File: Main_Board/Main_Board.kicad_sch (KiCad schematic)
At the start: 8 parts, among them U1 OKI-78SR-5_1.5-W36-C, U2 Teensy4.1_DEV-16771, U3 ATA6561

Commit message: **MAJOR CHANGES**
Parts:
- removed R1: 120ohm, symbol Device:R
- removed U3: ATA6561, Package_SO:SOIC-8_3.9x4.9mm_P1.27mm, symbol MRDT_Devices:ATA6561
- added 100nf: C, symbol Device:C
- added J1: RJ45_LED_Shielded, symbol Connector:RJ45_LED_Shielded
- added U3: AS5048A, Package_SO:TSSOP-14_4.4x5mm_P0.65mm, symbol Sensor_Magnetic:AS5048A
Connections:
- net +3.3V: no longer C2.1, C3.1, U1.3 (OUT)
- net GND: now also 100nf.2, J1.8, J1.9, J1.SH
- net LED: now reaches U2.LED
- net LED: now also J1.10
- net R+: now reaches U2.R+
- net R+: now also J1.4
- net R-: now reaches U2.R-
- net R-: now also J1.6
- net T+: now reaches U2.T+
- net T+: now also J1.1
- net T-: now reaches U2.T-
- net T-: now also J1.3
- net +12V renamed +36V
- net RXD1: no longer names the net of U2.0 (RX1)
- net RXD2: no longer names the net of U2.7 (RX2)
- net RXD3: no longer names the net of U2.28 (RX7)
- net STBY1: no longer names the net of U2.14 (A0)
- net STBY2: no longer names the net of U2.15 (A1)
- net STBY3: no longer names the net of U2.16 (A2)
- net TXD1: no longer names the net of U2.1 (TX1)
- net TXD2: no longer names the net of U2.8 (TX2)
- net TXD3: no longer names the net of U2.29 (TX7)
- new net: 100nf.1, J1.2, J1.5
- new net +3V3: C2.1, C3.1, U1.3 (OUT)
- no-connect marks 1 -> 3
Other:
- moved on the sheet: C1, C2, C3, C4, U1, U2

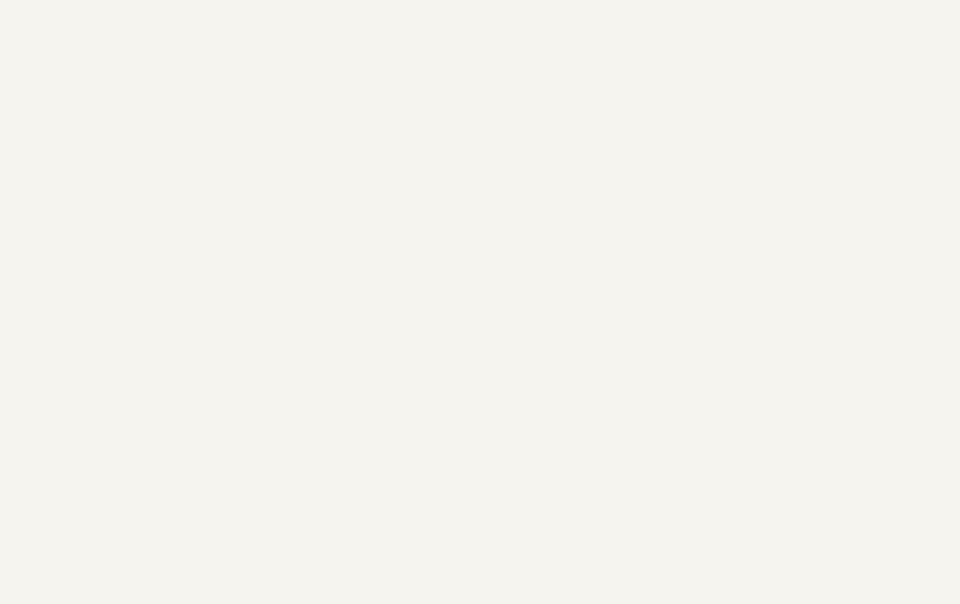
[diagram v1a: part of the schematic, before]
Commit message: Added Some UART Outputs
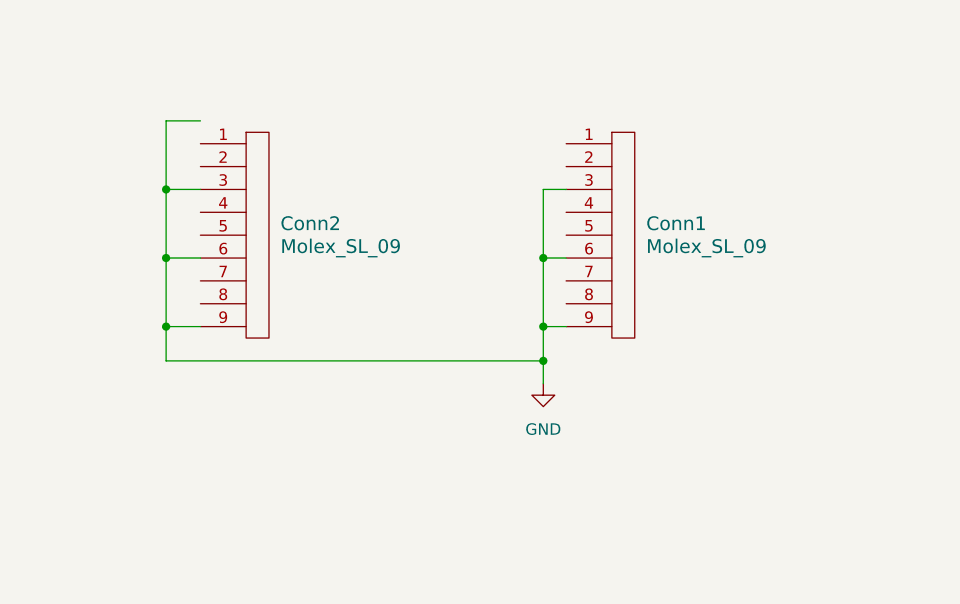
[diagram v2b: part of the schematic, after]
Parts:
- added Conn1, Conn2: Molex_SL_09, symbol MRDT_Connectors:Molex_SL_09
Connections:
- net GND: now also Conn1.3, Conn1.6, Conn1.9, Conn2.3, Conn2.6, Conn2.9

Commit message: Finished adding UART.
Find a 12 pin connector. Add buttons. Made a 4 nand gate symbol for buttons.
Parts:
- added SNx4HC1: ~, symbol MRDT_ICs:SNx4HC00
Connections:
- net J1RX: now reaches U2.0 (RX1)
- net J1TX: now reaches U2.1 (TX1)
- net J3TX: now reaches U2.14 (A0)
- net J3TX: now also Conn2.5
- net J3RX: now reaches U2.15 (A1)
- net J3RX: now also Conn2.4
- net J4RX: now reaches U2.16 (A2)
- net J4RX: now also Conn2.7
- net J4TX: now reaches U2.17 (A3)
- net J4TX: now also Conn2.8
- net J5TX: now reaches U2.20 (A6)
- net J5TX: now also Conn1.2
- net J5RX: now reaches U2.21 (A7)
- net J5RX: now also Conn1.1
- net J6RX: now reaches U2.28 (RX7)
- net J6RX: now also Conn1.4
- net J6TX: now reaches U2.29 (TX7)
- net J6TX: now also Conn1.5
- net J7RX: now reaches U2.34 (RX8)
- net J7RX: now also Conn1.7
- net J7TX: now reaches U2.35 (TX8)
- net J7TX: now also Conn1.8
- net J2RX: now reaches U2.7 (RX2)
- net J2RX: now also Conn2.1
- net J2TX: now reaches U2.8 (TX2)
- net J2TX: now also Conn2.2
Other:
- moved on the sheet: Conn1, Conn2

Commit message: Added Some More Button Options
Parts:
- added Conn3: AndersonPP, symbol MRDT_Connectors:AndersonPP
- added D1, D2, D3, D4, D5, D6, D7, D8, D9: BLUE, LED_SMD:LED_0603_1608Metric_Pad1.05x0.95mm_HandSolder, symbol Device:LED
- added D10, D11, D12, D13: YELLOW, LED_SMD:LED_0603_1608Metric_Pad1.05x0.95mm_HandSolder, symbol Device:LED
- added R1, R11, R13, R15, R18, R20, R22, R24, R3, R5, R7, R9: 4.7k, Resistor_SMD:R_0603_1608Metric_Pad0.98x0.95mm_HandSolder, symbol Device:R
- added R10, R12, R14, R16, R17, R19, R2, R21, R23, R25, R4, R6, R8: 120, Resistor_SMD:R_0603_1608Metric_Pad0.98x0.95mm_HandSolder, symbol Device:R
- added SW1, SW10, SW11, SW12, SW13, SW2, SW3, SW4, SW5, SW6, SW7, SW8: SW_Push, Button_Switch_SMD:SW_SPST_TL3305A, symbol Switch:SW_Push
- added SW9: SW_SPDT, Button_Switch_THT:SW_Slide_1P2T_CK_OS102011MS2Q, symbol Switch:SW_SPDT
- SNx4HC1: footprint (none) -> Package_SO:SO-14_5.3x10.2mm_P1.27mm
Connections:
- net +3V3: now also D1.2 (A), D10.2 (A), D11.2 (A), D12.2 (A), D13.2 (A), D2.2 (A), D3.2 (A), D4.2 (A), D5.2 (A), D6.2 (A), D7.2 (A), D8.2 (A), R1.1, R11.1, R13.1, R15.1, R18.1, R20.1, R22.1, R24.1, R3.1, R5.1, R7.1, R9.1, SW9.3 (C)
- net GND: now also D9.1 (K), SW1.1, SW10.1, SW11.1, SW12.1, SW13.1, SW2.1, SW3.1, SW4.1, SW5.1, SW6.1, SW7.1, SW8.1, SW9.1 (A)
- net REVERSE: now reaches U2.5 (IN2)
- net REVERSE: now also R17.2, SW9.2 (B)
- new net: D12.1 (K), R23.2
- new net: D3.1 (K), R6.2
- new net: D7.1 (K), R14.2
- new net: D10.1 (K), R19.2
- new net: D13.1 (K), R25.2
- new net: D5.1 (K), R10.2
- new net: D9.2 (A), R17.1
- new net: D1.1 (K), R2.2
- new net: D6.1 (K), R12.2
- new net: D8.1 (K), R16.2
- new net: D4.1 (K), R8.2
- new net: D2.1 (K), R4.2
- new net: D11.1 (K), R21.2
- new net B1: R1.2, R2.1, SW1.2
- new net B10: R20.2, R21.1, SW11.2
- new net B11: R22.2, R23.1, SW12.2
- new net B12: R24.2, R25.1, SW13.2
- new net B2: R3.2, R4.1, SW2.2
- new net B3: R5.2, R6.1, SW3.2
- new net B4: R7.2, R8.1, SW4.2
- new net B5: R10.1, R9.2, SW5.2
- new net B6: R11.2, R12.1, SW6.2
- new net B7: R13.2, R14.1, SW7.2
- new net B8: R15.2, R16.1, SW8.2
- new net B9: R18.2, R19.1, SW10.2
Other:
- moved on the sheet: C1, C2, C3, C4, U1

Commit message: Rev1 is awaiting review by lead
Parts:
- removed D10, D11, D12, D13: YELLOW, LED_SMD:LED_0603_1608Metric_Pad1.05x0.95mm_HandSolder, symbol Device:LED
- removed R18, R20, R22, R24: 4.7k, Resistor_SMD:R_0603_1608Metric_Pad0.98x0.95mm_HandSolder, symbol Device:R
- removed R19, R21, R23, R25: 120, Resistor_SMD:R_0603_1608Metric_Pad0.98x0.95mm_HandSolder, symbol Device:R
- removed SW10, SW11, SW12, SW13: SW_Push, Button_Switch_SMD:SW_SPST_TL3305A, symbol Switch:SW_Push
- added U4: 74HC148, Package_SO:SOIC-16_4.55x10.3mm_P1.27mm, symbol 74xx:74LS148
- added U6: 74HC00, Package_SO:SO-14_5.3x10.2mm_P1.27mm, symbol 74xx:74HC00
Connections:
- net +36V: now also Conn3.2 (V+Log)
- net +3V3: now also U4.16 (VCC)
- net B1: now also U4.10 (IO)
- net B2: now also U4.11 (I1)
- net B3: now also U4.12 (I2)
- net B4: now also U4.13 (I3)
- net B5: now also U4.1 (I4)
- net B6: now also U4.2 (I5)
- net B7: now also U4.3 (I6)
- net B8: now also U4.4 (I7)
- net GND: now also Conn3.1 (GND), U4.5 (EI), U4.8 (GND), U6.5
- net OUT0: now reaches U2.18 (A4)
- net OUT0: now also U6.3
- net OUT1: now reaches U2.19 (A5)
- net OUT1: now also U6.6
- new net: U4.6 (S2), U6.4
- new net: U4.7 (S1), U6.2
- new net: U4.9 (S0), U6.1
- no-connect marks 3 -> 62
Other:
- note added: "Encoders"
- moved on the sheet: 100nf, C1, C2, C3, C4, Conn1, Conn2, Conn3A, Conn3B, D1, D2, D3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
